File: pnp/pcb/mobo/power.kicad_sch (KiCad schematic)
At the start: 31 parts, among them J12 COMBO_POWER_JACK, U11 FDS4435BZ, U12 TPS54331, U13 AP1117-33, U6 Fuse_Holder_3568

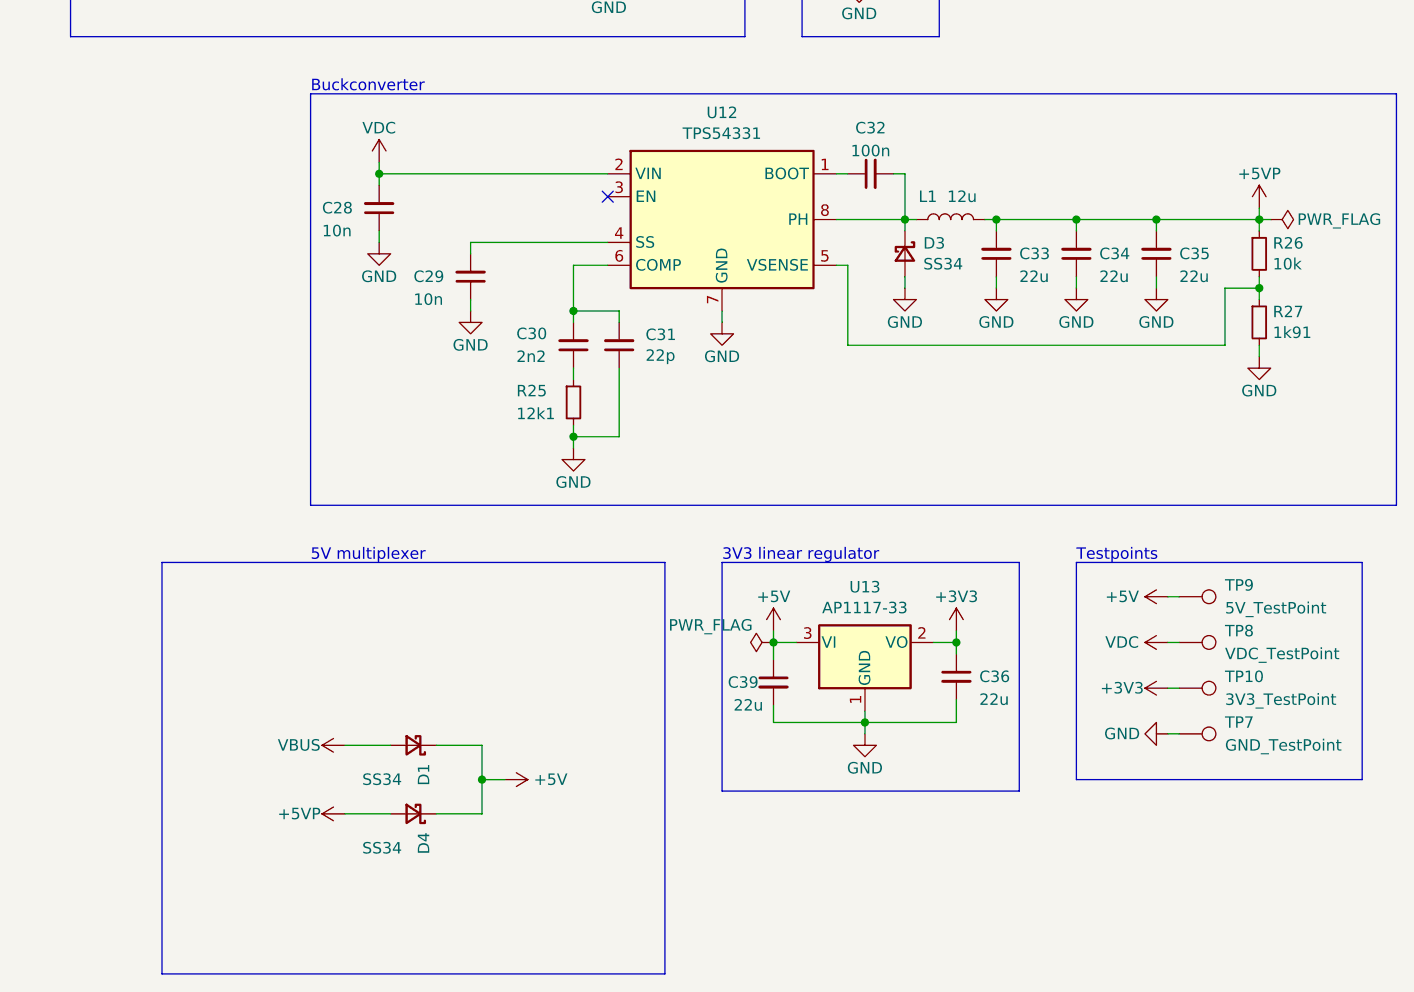
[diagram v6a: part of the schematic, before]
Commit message: removed 5vp rail and 5v multiplexer
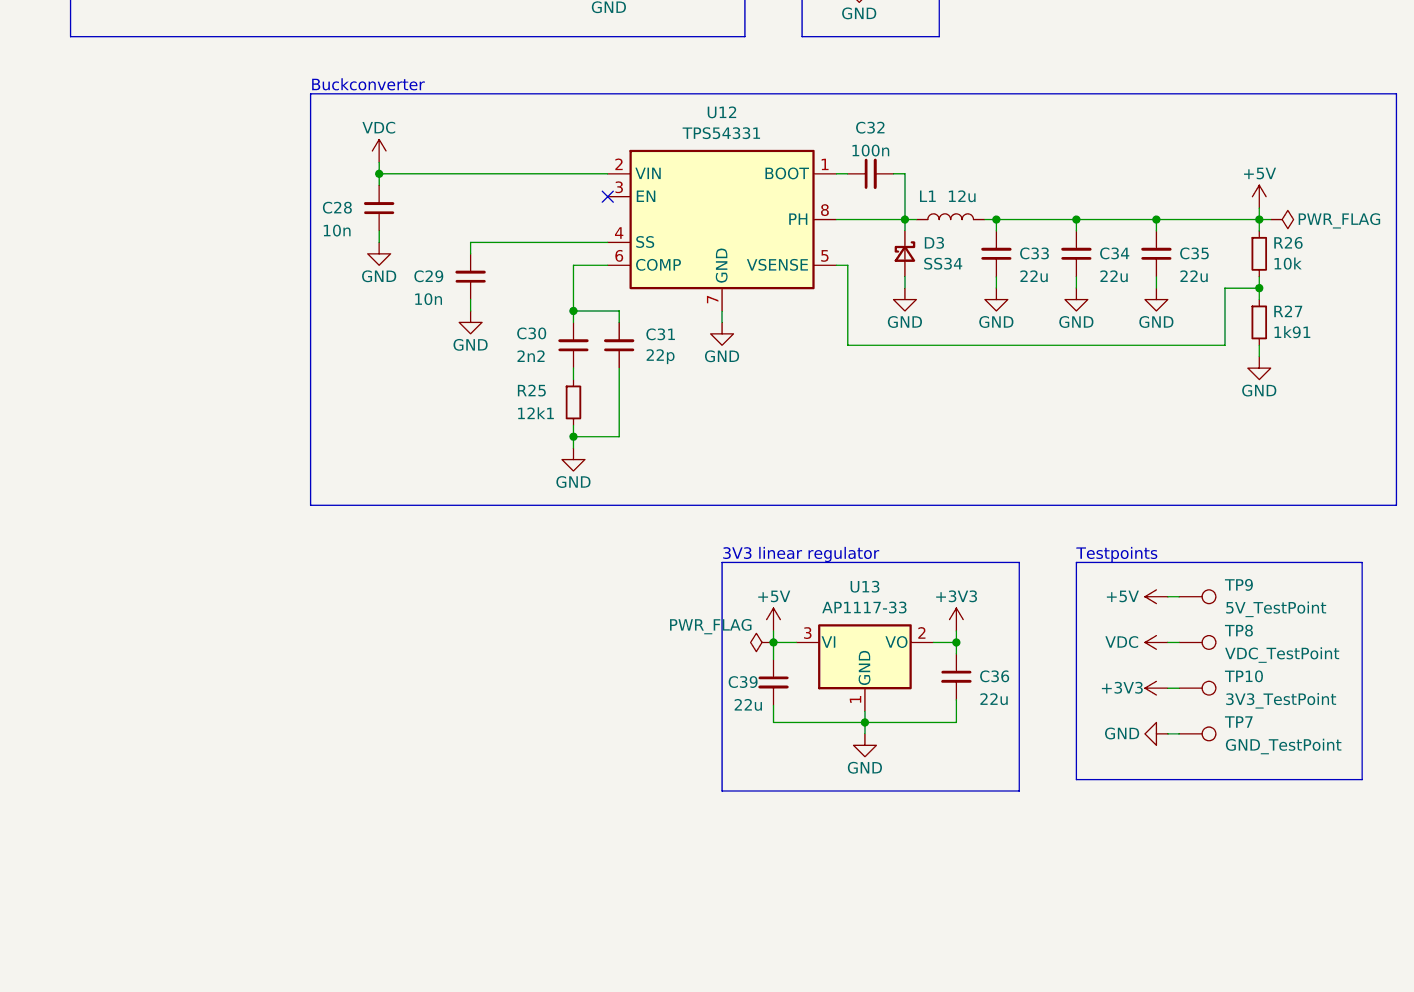
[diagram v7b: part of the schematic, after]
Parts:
- removed D1, D4: SS34, Diode_SMD:D_SMA, symbol Device:D_Schottky_Small
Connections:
- net +5VP is gone; now on net +5V: C33.2, C34.2, C35.2, L1.2, R26.1
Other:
- note removed: "5V multiplexer"
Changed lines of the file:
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@@
   (junction (at 150.495 149.86) (diameter 0) (color 0 0 0 0)
-  )
-  (junction (at 107.95 156.21) (diameter 0) (color 0 0 0 0)
   )
   (junction (at 118.11 104.14) (diameter 0) (color 0 0 0 0)
@@
     (stroke (width 0) (type default))
   )
-  (wire (pts (xy 107.95 160.02) (xy 107.95 156.21))
-    (stroke (width 0) (type default))
-  )
-  (wire (pts (xy 92.71 160.02) (xy 97.79 160.02))
-    (stroke (width 0) (type default))
-  )
   (polyline (pts (xy 158.75 46.99) (xy 158.75 73.66))
     (stroke (width 0) (type default))
   )
-  (polyline (pts (xy 72.39 132.08) (xy 128.27 132.08))
-    (stroke (width 0) (type default))
-  )
   (wire (pts (xy 96.52 95.25) (xy 96.52 96.52))
     (stroke (width 0) (type default))
@@
     (stroke (width 0) (type default))
   )
-  (wire (pts (xy 102.87 160.02) (xy 107.95 160.02))
-    (stroke (width 0) (type default))
-  )
   (wire (pts (xy 154.94 88.9) (xy 154.94 93.98))
     (stroke (width 0) (type default))
   )
-  (polyline (pts (xy 72.39 132.08) (xy 72.39 177.8))
-    (stroke (width 0) (type default))
-  )
   (wire (pts (xy 121.92 55.88) (xy 123.19 55.88))
     (stroke (width 0) (type default))
@@
     (stroke (width 0) (type default))
   )
-  (wire (pts (xy 102.87 152.4) (xy 107.95 152.4))
-    (stroke (width 0) (type default))
-  )
   (wire (pts (xy 140.335 147.955) (xy 140.335 149.86))
     (stroke (width 0) (type default))
@@
     (stroke (width 0) (type default))
   )
-  (polyline (pts (xy 128.27 177.8) (xy 72.39 177.8))
-    (stroke (width 0) (type default))
-  )
   (wire (pts (xy 154.94 93.98) (xy 154.94 95.25))
     (stroke (width 0) (type default))
@@
     (stroke (width 0) (type default))
   )
-  (wire (pts (xy 107.95 156.21) (xy 110.49 156.21))
-    (stroke (width 0) (type default))
-  )
   (wire (pts (xy 149.86 66.04) (xy 149.86 67.31))
     (stroke (width 0) (type default))
@@
     (stroke (width 0) (type default))
   )
-  (wire (pts (xy 107.95 152.4) (xy 107.95 156.21))
-    (stroke (width 0) (type default))
-  )
   (wire (pts (xy 160.655 139.7) (xy 160.655 140.97))
     (stroke (width 0) (type default))
@@
     (stroke (width 0) (type default))
   )
-  (wire (pts (xy 92.71 152.4) (xy 97.79 152.4))
-    (stroke (width 0) (type default))
-  )
   (wire (pts (xy 173.99 93.98) (xy 182.88 93.98))
     (stroke (width 0) (type default))
@@
   )
   (wire (pts (xy 86.995 30.48) (xy 86.995 34.925))
-    (stroke (width 0) (type default))
-  )
-  (polyline (pts (xy 128.27 132.08) (xy 128.27 177.8))
     (stroke (width 0) (type default))
   )
@@
   )
   (text "3V3 linear regulator" (at 134.62 132.08 0)
-    (effects (font (size 1.27 1.27)) (justify left bottom))
-  )
-  (text "5V multiplexer" (at 88.9 132.08 0)
     (effects (font (size 1.27 1.27)) (justify left bottom))
   )
@@
     )
   )
-  (symbol (lib_id "power:VBUS") (at 92.71 152.4 90) (unit 1)
-    (in_bom yes) (on_board yes) (dnp no)
-    (property "Reference" "#PWR0158" (at 96.52 152.4 0)
-      (effects (font (size 1.27 1.27)) hide)
-    )
-    (property "Value" "VBUS" (at 87.63 152.4 90)
-      (effects (font (size 1.27 1.27)))
-    )
-    (property "Footprint" "" (at 92.71 152.4 0)
-      (effects (font (size 1.27 1.27)) hide)
-    )
-    (property "Datasheet" "" (at 92.71 152.4 0)
-      (effects (font (size 1.27 1.27)) hide)
-    )
-    (pin "1")
-    (instances
-      (project "mobo"
-        (path "/7255cbd1-8d38-4545-be9a-7fc5488ef942/00000000-0000-0000-0000-00005eb15d5b"
-          (reference "#PWR0158") (unit 1)
-        )
-      )
-    )
-  )
   (symbol (lib_id "power:PWR_FLAG") (at 195.58 93.98 270) (unit 1)
     (in_bom yes) (on_board yes) (dnp no)
@@
     )
   )
-  (symbol (lib_id "Device:D_Schottky_Small") (at 100.33 152.4 180) (unit 1)
-    (in_bom yes) (on_board yes) (dnp no)
-    (property "Reference" "D1" (at 101.4984 154.432 90)
-      (effects (font (size 1.27 1.27)) (justify left))
-    )
-    (property "Value" "SS34" (at 99.06 156.21 0)
-      (effects (font (size 1.27 1.27)) (justify left))
-    )
-    (property "Footprint" "Diode_SMD:D_SMA" (at 100.33 152.4 0)
-      (effects (font (size 1.27 1.27)) hide)
-    )
-    (property "Datasheet" "~" (at 100.33 152.4 0)
-      (effects (font (size 1.27 1.27)) hide)
-    )
-    (property "LCSC" "C266553" (at 100.33 152.4 90)
-      (effects (font (size 1.27 1.27)) hide)
-    )
-    (property "JLCPCB" "C8678" (at 100.33 152.4 90)
-      (effects (font (size 1.27 1.27)) hide)
-    )
-    (property "Notes" "40V/3A" (at 100.33 152.4 90)
-      (effects (font (size 1.27 1.27)) hide)
-    )
-    (property "Config" "" (at 100.33 152.4 0)
-      (effects (font (size 1.27 1.27)) hide)
-    )
-    (property "Digikey" "641-2115-1-ND" (at 100.33 152.4 0)
-      (effects (font (size 1.27 1.27)) hide)
-    )
-    (property "Mouser" "821-SS34LRVG" (at 100.33 152.4 0)
-      (effects (font (size 1.27 1.27)) hide)
-    )
-    (pin "1")
-    (pin "2")
-    (instances
-      (project "mobo"
-        (path "/7255cbd1-8d38-4545-be9a-7fc5488ef942/00000000-0000-0000-0000-00005eb15d5b"
-          (reference "D1") (unit 1)
-        )
-      )
-    )
-  )
   (symbol (lib_id "power:VDC") (at 121.92 54.61 0) (unit 1)
     (in_bom yes) (on_board yes) (dnp no)
@@
         (path "/7255cbd1-8d38-4545-be9a-7fc5488ef942/00000000-0000-0000-0000-00005eb15d5b"
           (reference "#PWR0246") (unit 1)
+        )
+      )
+    )
+  )
+  (symbol (lib_id "power:+5V") (at 194.31 92.71 0) (unit 1)
+    (in_bom yes) (on_board yes) (dnp no)
+    (property "Reference" "#PWR03" (at 194.31 96.52 0)
+      (effects (font (size 1.27 1.27)) hide)
+    )
+    (property "Value" "+5V" (at 194.31 88.9 0)
+      (effects (font (size 1.27 1.27)))
+    )
+    (property "Footprint" "" (at 194.31 92.71 0)
+      (effects (font (size 1.27 1.27)) hide)
+    )
+    (property "Datasheet" "" (at 194.31 92.71 0)
+      (effects (font (size 1.27 1.27)) hide)
+    )
+    (pin "1")
+    (instances
+      (project "mobo"
+        (path "/7255cbd1-8d38-4545-be9a-7fc5488ef942/00000000-0000-0000-0000-00005eb15d5b"
+          (reference "#PWR03") (unit 1)
         )
       )
@@
     )
   )
-  (symbol (lib_id "power:+5VP") (at 194.31 92.71 0) (unit 1)
-    (in_bom yes) (on_board yes) (dnp no)
-    (property "Reference" "#PWR0244" (at 194.31 96.52 0)
-      (effects (font (size 1.27 1.27)) hide)
-    )
-    (property "Value" "+5VP" (at 194.31 88.9 0)
-      (effects (font (size 1.27 1.27)))
-    )
-    (property "Footprint" "" (at 194.31 92.71 0)
-      (effects (font (size 1.27 1.27)) hide)
-    )
-    (property "Datasheet" "" (at 194.31 92.71 0)
-      (effects (font (size 1.27 1.27)) hide)
-    )
-    (pin "1")
-    (instances
-      (project "mobo"
-        (path "/7255cbd1-8d38-4545-be9a-7fc5488ef942/00000000-0000-0000-0000-00005eb15d5b"
-          (reference "#PWR0244") (unit 1)
-        )
-      )
-    )
-  )
   (symbol (lib_id "power:PWR_FLAG") (at 140.335 140.97 90) (unit 1)
     (in_bom yes) (on_board yes) (dnp no)
@@
         )
       )
-    )
-  )
-  (symbol (lib_id "power:+5VP") (at 92.71 160.02 90) (unit 1)
-    (in_bom yes) (on_board yes) (dnp no)
-    (property "Reference" "#PWR0245" (at 96.52 160.02 0)
-      (effects (font (size 1.27 1.27)) hide)
-    )
-    (property "Value" "+5VP" (at 87.63 160.02 90)
-      (effects (font (size 1.27 1.27)))
-    )
-    (property "Footprint" "" (at 92.71 160.02 0)
-      (effects (font (size 1.27 1.27)) hide)
-    )
-    (property "Datasheet" "" (at 92.71 160.02 0)
-      (effects (font (size 1.27 1.27)) hide)
-    )
-    (pin "1")
-    (instances
-      (project "mobo"
-        (path "/7255cbd1-8d38-4545-be9a-7fc5488ef942/00000000-0000-0000-0000-00005eb15d5b"
-          (reference "#PWR0245") (unit 1)
-        )
-      )
-    )
-  )
-  (symbol (lib_id "power:+5V") (at 110.49 156.21 270) (unit 1)
-    (in_bom yes) (on_board yes) (dnp no)
-    (property "Reference" "#PWR0116" (at 106.68 156.21 0)
-      (effects (font (size 1.27 1.27)) hide)
-    )
-    (property "Value" "+5V" (at 115.57 156.21 90)
-      (effects (font (size 1.27 1.27)))
-    )
-    (property "Footprint" "" (at 110.49 156.21 0)
-      (effects (font (size 1.27 1.27)) hide)
-    )
-    (property "Datasheet" "" (at 110.49 156.21 0)
-      (effects (font (size 1.27 1.27)) hide)
-    )
-    (pin "1")
-    (instances
-      (project "mobo"
-        (path "/7255cbd1-8d38-4545-be9a-7fc5488ef942/00000000-0000-0000-0000-00005eb15d5b"
-          (reference "#PWR0116") (unit 1)
-        )
-      )
-    )
-  )
-  (symbol (lib_id "Device:D_Schottky_Small") (at 100.33 160.02 180) (unit 1)
-    (in_bom yes) (on_board yes) (dnp no)
-    (property "Reference" "D4" (at 101.4984 162.052 90)
-      (effects (font (size 1.27 1.27)) (justify left))
-    )
-    (property "Value" "SS34" (at 99.06 163.83 0)
-      (effects (font (size 1.27 1.27)) (justify left))
-    )
-    (property "Footprint" "Diode_SMD:D_SMA" (at 100.33 160.02 0)
-      (effects (font (size 1.27 1.27)) hide)
-    )
-    (property "Datasheet" "~" (at 100.33 160.02 0)
-      (effects (font (size 1.27 1.27)) hide)
-    )
-    (property "LCSC" "C266553" (at 100.33 160.02 90)
-      (effects (font (size 1.27 1.27)) hide)
-    )
-    (property "JLCPCB" "C8678" (at 100.33 160.02 90)
-      (effects (font (size 1.27 1.27)) hide)
-    )
-    (property "Notes" "40V/3A" (at 100.33 160.02 90)
-      (effects (font (size 1.27 1.27)) hide)
-    )
-    (property "Config" "" (at 100.33 160.02 0)
-      (effects (font (size 1.27 1.27)) hide)
-    )
-    (property "Digikey" "641-2115-1-ND" (at 100.33 160.02 0)
-      (effects (font (size 1.27 1.27)) hide)
-    )
-    (property "Mouser" "821-SS34LRVG" (at 100.33 160.02 0)
-      (effects (font (size 1.27 1.27)) hide)
-    )
-    (pin "1")
-    (pin "2")
-    (instances
-      (project "mobo"
-        (path "/7255cbd1-8d38-4545-be9a-7fc5488ef942/00000000-0000-0000-0000-00005eb15d5b"
-          (reference "D4") (unit 1)
-        )
-      )
